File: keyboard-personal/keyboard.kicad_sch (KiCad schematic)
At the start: 173 parts, among them J1 USB_B_Mini, U1 ATmega168PA-A, U2 CH340C, U3 74HC154D, U4 74HC4051, Y1 16MHz

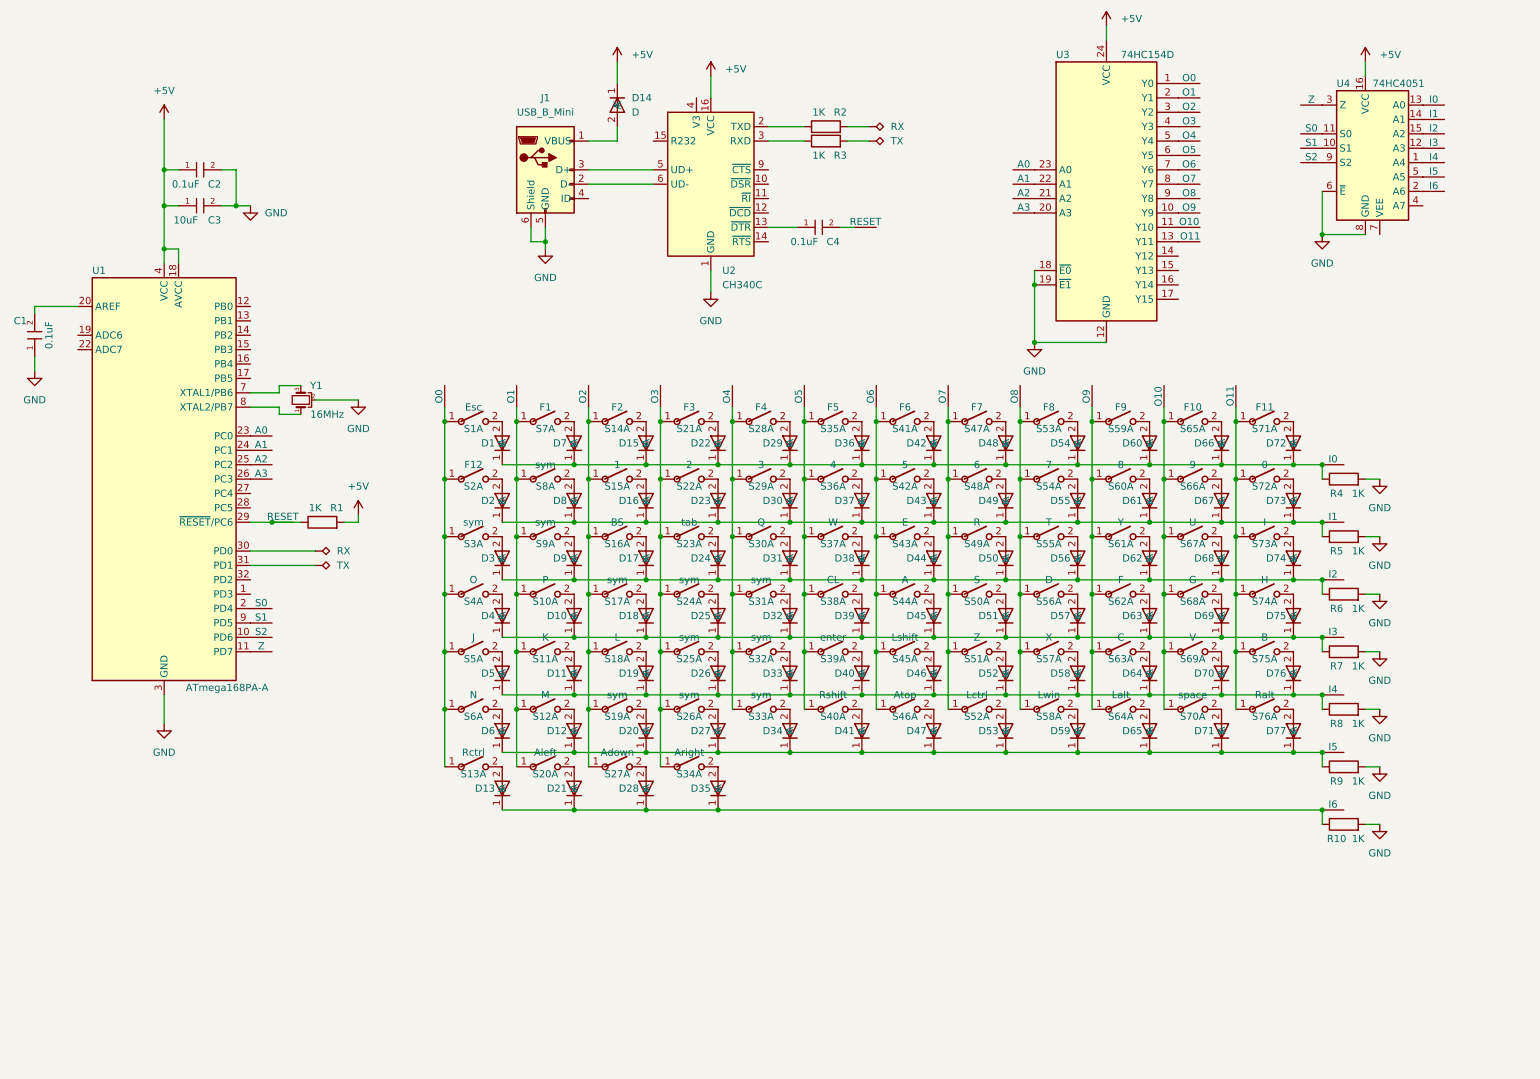
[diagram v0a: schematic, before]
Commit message: Update latest version of keyboard-personal
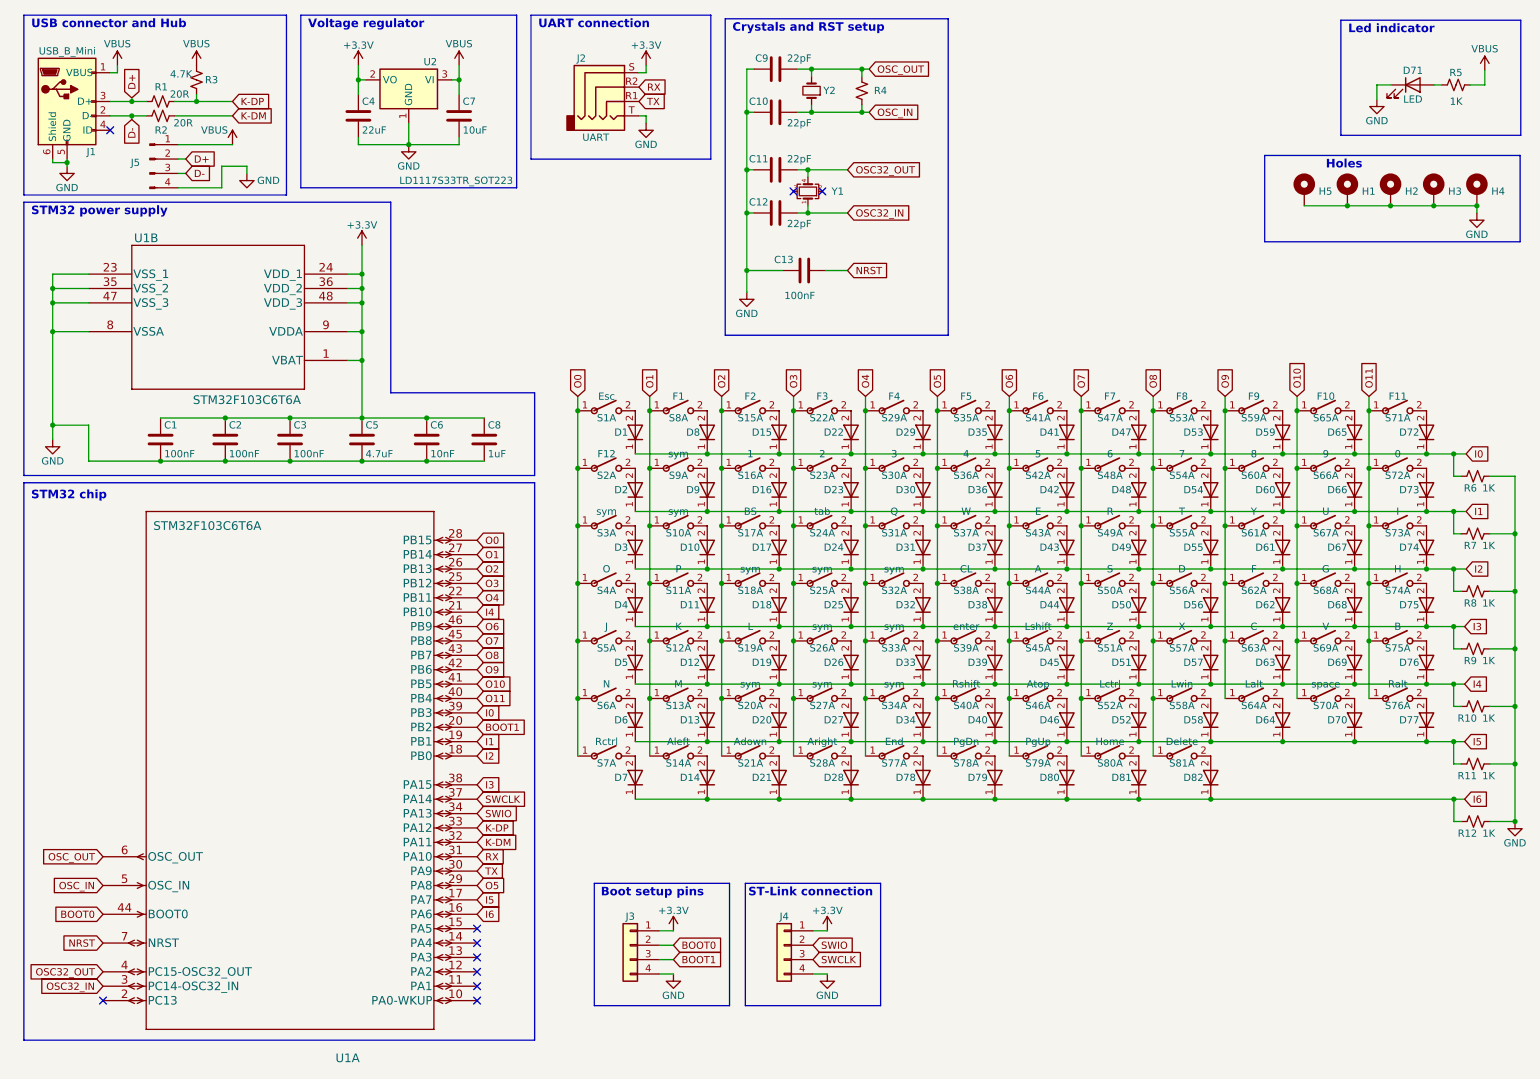
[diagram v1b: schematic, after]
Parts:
- removed C1, C2, C4: 0.1uF, common:C_1206_3216Metric, symbol symbols:C
- removed C3: 10uF, common:C_1206_3216Metric, symbol symbols:C
- removed D14: D, common:D_0603_1608Metric, symbol symbols:D
- removed R1, R10, R2, R3, R4, R5, R6, R7, R8, R9: 1K, common:R_0603_1608Metric, symbol symbols:R
- removed U1: ATmega168PA-A, Package_QFP:TQFP-32_7x7mm_P0.8mm, symbol symbols:ATmega168PA-A
- removed U2: CH340C, Package_SO:SOIC-16_3.9x9.9mm_P1.27mm, symbol symbols:CH340C
- removed U3: 74HC154D, common:SSOP-24_3.9x8.7mm_P0.635mm, symbol symbols:74HC154D
- removed U4: 74HC4051, common:SSOP-16_3.9x4.9mm_P0.635mm, symbol symbols:74HC4051
- removed Y1: 16MHz, common:Resonator_SMD_Murata_CSTxExxV-3Pin_3.0x1.1mm, symbol symbols:Crystal_GND2_Small
- added C1, C13, C2, C3: 100nF, Capacitor_SMD:C_0805_2012Metric, symbol Device:C
- added C10, C11, C12, C9: 22pF, Capacitor_SMD:C_0805_2012Metric, symbol Device:C
- added C4: 22uF, Capacitor_SMD:C_1206_3216Metric, symbol Device:C
- added C5: 4.7uF, Capacitor_SMD:C_0805_2012Metric, symbol Device:C
- added C6: 10nF, Capacitor_SMD:C_0805_2012Metric, symbol Device:C
- added C7: 10uF, Capacitor_SMD:C_1206_3216Metric, symbol Device:C
- added C8: 1uF, Capacitor_SMD:C_0805_2012Metric, symbol Device:C
- added D71: LED, LED_SMD:LED_0805_2012Metric, symbol Device:LED
- added D78, D79, D80, D81, D82: D, common:D_0603_1608Metric, symbol symbols:D
- added H1, H2, H3, H4, H5: MountingHole, MountingHole:MountingHole_3.2mm_M3_DIN965_Pad, symbol Mechanical:MountingHole_Pad
- added J2: UART, common:PJ320D, symbol Connector:AudioJack4
- added J3, J4: Conn_01x04, Connector_PinHeader_2.54mm:PinHeader_1x04_P2.54mm_Vertical, symbol Connector_Generic:Conn_01x04
- added J5: Conn_01x04_Pin, Connector_PinSocket_1.27mm:PinSocket_1x04_P1.27mm_Vertical, symbol Connector:Conn_01x04_Pin
- added R1, R2: 20R, Resistor_SMD:R_0805_2012Metric, symbol Device:R_Small_US
- added R10, R11, R12, R5, R6, R7, R8, R9: 1K, Resistor_SMD:R_0805_2012Metric, symbol Device:R_Small_US
- added R3: 4.7K, Resistor_SMD:R_0805_2012Metric, symbol Device:R_Small_US
- added R4: R_Small_US, Resistor_SMD:R_0805_2012Metric, symbol Device:R_Small_US
- added S77: End, Switch_Keyboard_Cherry_MX:SW_Cherry_MX_PCB_1.00u, symbol symbols:Switch
- added S78: PgDn, Switch_Keyboard_Cherry_MX:SW_Cherry_MX_PCB_1.00u, symbol symbols:Switch
- added S79: PgUp, Switch_Keyboard_Cherry_MX:SW_Cherry_MX_PCB_1.00u, symbol symbols:Switch
- added S80: Home, Switch_Keyboard_Cherry_MX:SW_Cherry_MX_PCB_1.00u, symbol symbols:Switch
- added S81: Delete, Switch_Keyboard_Cherry_MX:SW_Cherry_MX_PCB_1.00u, symbol symbols:Switch
- added U1: STM32F103C6T6A, Package_QFP:LQFP-48_7x7mm_P0.5mm, symbol STM32F103C6T6A:STM32F103C6T6A
- added U2: LD1117S33TR_SOT223, Package_TO_SOT_SMD:SOT-223-3_TabPin2, symbol Regulator_Linear:LD1117S33TR_SOT223
- added Y1: Crystal_GND23_Small, Crystal:Crystal_SMD_SeikoEpson_MC306-4Pin_8.0x3.2mm, symbol Device:Crystal_GND23_Small
- added Y2: Crystal_Small, Crystal:Crystal_SMD_Abracon_ABM3-2Pin_5.0x3.2mm, symbol Device:Crystal_Small
- J1: footprint common:USB_Micro-B_GCT_USB3076-30-A -> common:USB_Micro-B_A01SB141B1-245
- S17: renamed from S16; footprint Switch_Keyboard_Cherry_MX:SW_Cherry_MX_PCB_1.00u -> Switch_Keyboard_Cherry_MX:SW_Cherry_MX_PCB_2.00u
- S24: renamed from S23; footprint Switch_Keyboard_Cherry_MX:SW_Cherry_MX_PCB_1.00u -> Switch_Keyboard_Cherry_MX:SW_Cherry_MX_PCB_1.50u
- S32: renamed from S31; footprint Switch_Keyboard_Cherry_MX:SW_Cherry_MX_PCB_1.00u -> Switch_Keyboard_Cherry_MX:SW_Cherry_MX_PCB_1.50u
- S38, S40: footprint Switch_Keyboard_Cherry_MX:SW_Cherry_MX_PCB_1.00u -> Switch_Keyboard_Cherry_MX:SW_Cherry_MX_PCB_1.75u
- S39: footprint Switch_Keyboard_Cherry_MX:SW_Cherry_MX_PCB_2.00u -> Switch_Keyboard_Cherry_MX:SW_Cherry_MX_PCB_2.25u
- S45: footprint Switch_Keyboard_Cherry_MX:SW_Cherry_MX_PCB_1.00u -> Switch_Keyboard_Cherry_MX:SW_Cherry_MX_PCB_2.25u
- S52, S58, S64, S76: footprint Switch_Keyboard_Cherry_MX:SW_Cherry_MX_PCB_1.00u -> Switch_Keyboard_Cherry_MX:SW_Cherry_MX_PCB_1.25u
- S7: renamed from S13; footprint Switch_Keyboard_Cherry_MX:SW_Cherry_MX_PCB_1.00u -> Switch_Keyboard_Cherry_MX:SW_Cherry_MX_PCB_1.25u
- S70: footprint Switch_Keyboard_Cherry_MX:SW_Cherry_MX_PCB_6.00u -> Switch_Keyboard_Cherry_MX:SW_Cherry_MX_PCB_6.25u
- renumbered D9 to D10, D10 to D11, D11 to D12, D12 to D13, D21 to D14, D28 to D21, D35 to D28, D36 to D35, D37 to D36, D38 to D37, D39 to D38, D40 to D39, D41 to D40, D42 to D41, D43 to D42, D44 to D43, D45 to D44, D46 to D45, D47 to D46, D48 to D47, D49 to D48, D50 to D49, D51 to D50, D52 to D51, D53 to D52, D54 to D53, D55 to D54, D56 to D55, D57 to D56, D58 to D57, D59 to D58, D60 to D59, D61 to D60, D62 to D61, D63 to D62, D64 to D63, D65 to D64, D66 to D65, D67 to D66, D68 to D67, D69 to D68, D70 to D69, D13 to D7, D71 to D70, D7 to D8, D8 to D9, S9 to S10, S10 to S11, S11 to S12, S12 to S13, S20 to S14, S14 to S15, S15 to S16, S17 to S18, S18 to S19, S19 to S20, S27 to S21, S21 to S22, S22 to S23, S24 to S25, S25 to S26, S26 to S27, S34 to S28, S28 to S29, S29 to S30, S30 to S31, S32 to S33, S33 to S34, S7 to S8, S8 to S9
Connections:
- net GND: now also C1.2, C10.1, C11.1, C12.1, C13.1, C2.2, C3.2, C4.2, C5.2, C6.2, C7.2, C8.2, C9.1, D71.1 (K), H1.1, H2.1, H3.1, H4.1, H5.1, J2.T, J3.4 (Pin_4), J4.4 (Pin_4), J5.4 (Pin_4), R10.2, R11.2, R12.2, R6.2, R7.2, R8.2, R9.2, U1.23 (VSS_1), U1.35 (VSS_2), U1.47 (VSS_3), U1.8 (VSSA), U2.1 (GND)
- net I0: now also R6.1, U1.39 (PB3)
- net I1: now also R7.1, U1.19 (PB1)
- net I2: now also R8.1, U1.18 (PB0)
- net I3: now also R9.1, U1.38 (PA15)
- net I4: now also R10.1, U1.21 (PB10)
- net I5: now also R11.1, U1.17 (PA7)
- net I6: now also D78.1, D79.1, D80.1, D81.1, D82.1, R12.1, U1.16 (PA6)
- net O0: now also U1.28 (PB15)
- net O1: now also U1.27 (PB14)
- net O10: now also U1.41 (PB5)
- net O11: now also U1.40 (PB4)
- net O2: now also U1.26 (PB13)
- net O3: now also U1.25 (PB12)
- net O4: now also S77.1, U1.22 (PB11)
- net O5: now also S78.1, U1.29 (PA8)
- net O6: now also S79.1, U1.46 (PB9)
- net O7: now also S80.1, U1.45 (PB8)
- net O8: now also S81.1, U1.43 (PB7)
- net O9: now also U1.42 (PB6)
- net RX: now also J2.R2, U1.31 (PA10)
- net TX: now also J2.R1, U1.30 (PA9)
- net VBUS: now reaches J1.1 (VBUS)
- net VBUS: now also C7.1, J5.1 (Pin_1), R3.2, R5.2, U2.3 (VI)
- net D-: now reaches J1.2 (D-)
- net D-: now also J5.3 (Pin_3), R2.1
- net D+: now reaches J1.3 (D+)
- net D+: now also J5.2 (Pin_2), R1.1
- new net: D80.2, S79.2
- new net: D71.2 (A), R5.1
- new net: D81.2, S80.2
- new net: D78.2, S77.2
- new net: D79.2, S78.2
- new net: D82.2, S81.2
- new net +3.3V: C1.1, C2.1, C3.1, C4.1, C5.1, C6.1, C8.1, J2.S, J3.1 (Pin_1), J4.1 (Pin_1), U1.1 (VBAT), U1.24 (VDD_1), U1.36 (VDD_2), U1.48 (VDD_3), U1.9 (VDDA), U2.2 (VO)
- new net BOOT0: J3.2 (Pin_2), U1.44 (BOOT0)
- new net BOOT1: J3.3 (Pin_3), U1.20 (PB2)
- new net K-DM: R2.2, U1.32 (PA11)
- new net K-DP: R1.2, R3.1, U1.33 (PA12)
- new net NRST: C13.2, U1.7 (NRST)
- new net OSC32_IN: C12.2, U1.3 (PC14-OSC32_IN), Y1.1
- new net OSC32_OUT: C11.2, U1.4 (PC15-OSC32_OUT), Y1.4
- new net OSC_IN: C10.2, R4.1, U1.5 (OSC_IN), Y2.1
- new net OSC_OUT: C9.2, R4.2, U1.6 (OSC_OUT), Y2.2
- new net SWCLK: J4.3 (Pin_3), U1.37 (PA14)
- new net SWIO: J4.2 (Pin_2), U1.34 (PA13)
- no-connect marks 0 -> 10
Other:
- note added: "Boot setup pins"
- note added: "Crystals and RST setup"
- note added: "Holes"
- note added: "Led indicator"
- note added: "ST-Link connection"
- note added: "STM32 chip"
- note added: "STM32 power supply"
- note added: "UART connection"
- note added: "USB connector and Hub"
- note added: "Voltage regulator"
- title: Arduino Keyboard -> STM32 Keyboard
- moved on the sheet: S10A, S11A, S12A, S13A, S14A, S15A, S16A, S17A, S18A, S19A, S1A, S20A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
